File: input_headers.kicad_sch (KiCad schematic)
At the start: 22 parts, among them J1 171857-0003, J2 171856-0002, J6 171856-0002, J7 Conn_01x07, J8 USB_B_Micro, J9 TLW-104-05-T-D, U3 FT230XS-R

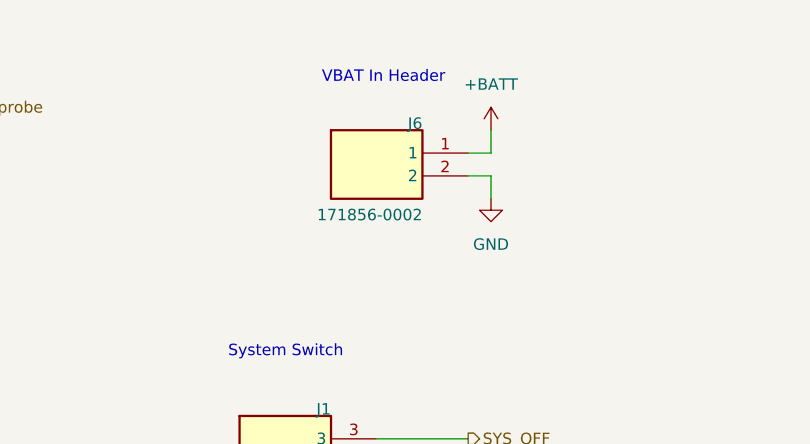
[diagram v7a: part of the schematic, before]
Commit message: Removed battery power and input header
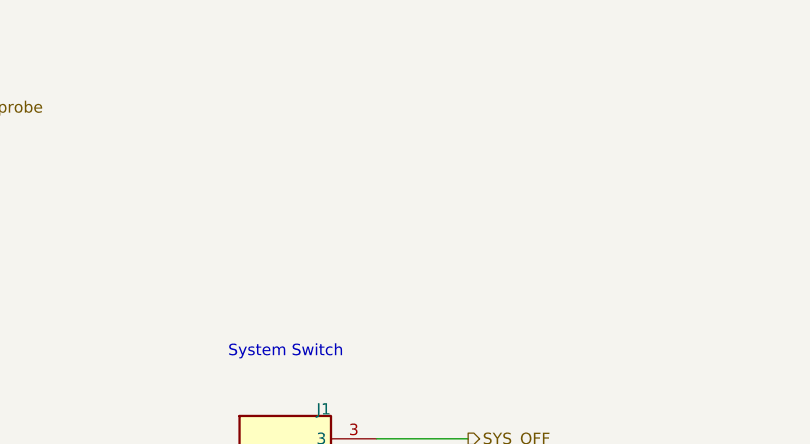
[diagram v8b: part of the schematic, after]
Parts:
- removed J6: 171856-0002, AltiumImport:SHDR2W99P0X254_1X2_493X635X818P, symbol MEB-altium-import:power_regulation_0_171856-0002
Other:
- note removed: "VBAT In Header"
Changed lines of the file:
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@@
     (stroke (width 0) (type default))
-  )
-  (wire (pts (xy 107.95 33.02) (xy 107.95 30.48))
-    (stroke (width 0.254) (type default))
   )
   (wire (pts (xy 11.43 33.02) (xy 13.97 33.02))
@@
     (stroke (width 0) (type default))
   )
-  (wire (pts (xy 107.95 35.56) (xy 107.95 38.1))
-    (stroke (width 0.254) (type default))
-  )
   (wire (pts (xy 11.43 35.56) (xy 11.43 45.72))
     (stroke (width 0) (type default))
@@
     (stroke (width 0) (type default))
   )
-  (wire (pts (xy 105.41 33.02) (xy 107.95 33.02))
-    (stroke (width 0.254) (type default))
-  )
   (wire (pts (xy 99.06 67.31) (xy 95.25 67.31))
     (stroke (width 0) (type default))
@@
   (wire (pts (xy 190.5 124.46) (xy 190.5 120.65))
     (stroke (width 0) (type default))
-  )
-  (wire (pts (xy 105.41 35.56) (xy 107.95 35.56))
-    (stroke (width 0.254) (type default))
   )
   (wire (pts (xy 127 167.64) (xy 124.46 167.64))
@@
     (fill (type none))
     (effects (font (size 1.27 1.27)) (justify left top))
-  )
-  (text "VBAT In Header" (at 102.87 25.4 0)
-    (effects (font (size 1.27 1.27)) (justify right bottom))
   )
   (text "Kill Switch" (at 33.02 52.07 0)
@@
     )
   )
-  (symbol (lib_id "power:+BATT") (at 107.95 30.48 0) (unit 1)
-    (in_bom yes) (on_board yes) (dnp no) (fields_autoplaced)
-    (property "Reference" "#PWR041" (at 107.95 34.29 0)
-      (effects (font (size 1.27 1.27)) hide)
-    )
-    (property "Value" "+BATT" (at 107.95 25.4 0)
-      (effects (font (size 1.27 1.27)))
-    )
-    (property "Footprint" "" (at 107.95 30.48 0)
-      (effects (font (size 1.27 1.27)) hide)
-    )
-    (property "Datasheet" "" (at 107.95 30.48 0)
-      (effects (font (size 1.27 1.27)) hide)
-    )
-    (pin "1")
-    (instances
-      (project "MEB"
-        (path "/228e4997-23c1-4c21-939b-583cad26a5e3"
-          (reference "#PWR041") (unit 1)
-        )
-        (path "/228e4997-23c1-4c21-939b-583cad26a5e3/3aab6a70-cc66-4393-a750-92acad576aaa"
-          (reference "#PWR02") (unit 1)
-        )
-      )
-    )
-  )
   (symbol (lib_id "MEB-altium-import:leak_sensor_0_Header 4X2") (at 19.05 25.4 0) (unit 1)
     (in_bom yes) (on_board yes) (dnp no)
@@
     )
   )
-  (symbol (lib_id "power:GND") (at 107.95 38.1 0) (unit 1)
-    (in_bom yes) (on_board yes) (dnp no) (fields_autoplaced)
-    (property "Reference" "#PWR01" (at 107.95 44.45 0)
-      (effects (font (size 1.27 1.27)) hide)
-    )
-    (property "Value" "GND" (at 107.95 43.18 0)
-      (effects (font (size 1.27 1.27)))
-    )
-    (property "Footprint" "" (at 107.95 38.1 0)
-      (effects (font (size 1.27 1.27)) hide)
-    )
-    (property "Datasheet" "" (at 107.95 38.1 0)
-      (effects (font (size 1.27 1.27)) hide)
-    )
-    (pin "1")
-    (instances
-      (project "MEB"
-        (path "/228e4997-23c1-4c21-939b-583cad26a5e3/3aab6a70-cc66-4393-a750-92acad576aaa"
-          (reference "#PWR01") (unit 1)
-        )
-      )
-    )
-  )
   (symbol (lib_id "Device:R_US") (at 110.49 132.08 90) (unit 1)
     (in_bom yes) (on_board yes) (dnp no)
@@
         )
       )
-    )
-  )
-  (symbol (lib_id "MEB-altium-import:power_regulation_0_171856-0002") (at 105.41 33.02 0) (mirror y) (unit 1)
-    (in_bom yes) (on_board yes) (dnp no)
-    (property "Reference" "J6" (at 100.33 30.48 0)
-      (effects (font (size 1.27 1.27)) (justify left bottom))
-    )
-    (property "Value" "171856-0002" (at 100.33 40.64 0)
-      (effects (font (size 1.27 1.27)) (justify left bottom))
-    )
-    (property "Footprint" "AltiumImport:SHDR2W99P0X254_1X2_493X635X818P" (at 105.41 33.02 0)
-      (effects (font (size 1.27 1.27)) hide)
-    )
-    (property "Datasheet" "" (at 105.41 33.02 0)
-      (effects (font (size 1.27 1.27)) hide)
-    )
-    (property "Part Number" "171856-0002" (at 105.41 33.02 0)
-      (effects (font (size 1.27 1.27)) hide)
-    )
-    (pin "1")
-    (pin "2")
-    (instances
-      (project "MEB"
-        (path "/228e4997-23c1-4c21-939b-583cad26a5e3/90a8e139-216e-4b02-83ea-4edb1f5f4c15"
-          (reference "J6") (unit 1)
-        )
-        (path "/228e4997-23c1-4c21-939b-583cad26a5e3/3aab6a70-cc66-4393-a750-92acad576aaa"
-          (reference "J4") (unit 1)
-        )
-      )
